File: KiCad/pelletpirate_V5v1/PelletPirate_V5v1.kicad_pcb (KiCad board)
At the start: 2 copper layers, 65 x 110 mm, 136 parts, among them J1 SJ1-3523NG_Jack_PP, J2 SJ1-3523NG_Jack_PP, J3 SJ1-3523NG_Jack_PP, J4 SJ1-3523NG_Jack_PP, J5 SJ1-3523NG_Jack_PP, J6 Conn_01x04, J7 Conn_01x04_Socket, J8 USB4145-03-0170-C, J9 TB002-500-02BE, T1 BTA12-600BWRG, T2 BTA12-600BWRG, T3 BTA12-600BWRG, U1 USBLC6-2SC6, U3 H11AA1M

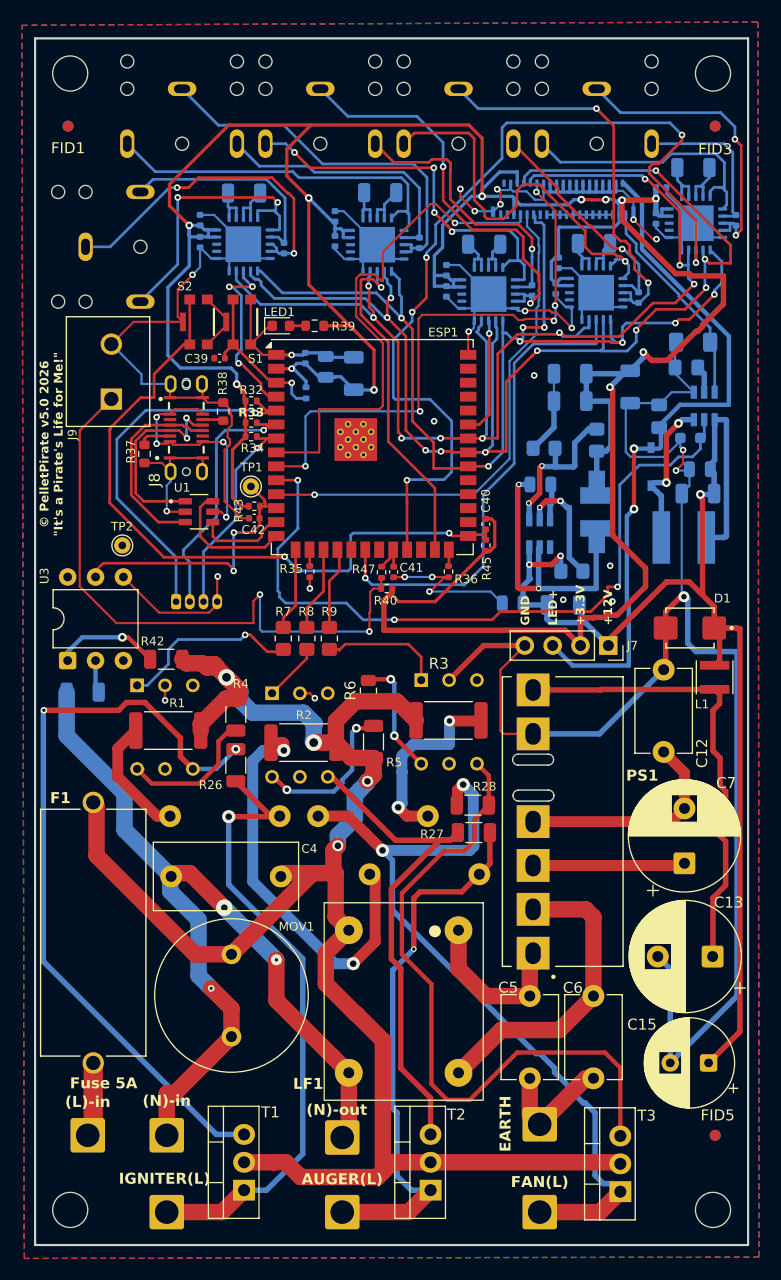
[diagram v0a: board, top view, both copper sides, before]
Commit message: V5v1 re-cloned fresh from as-ordered V5 (supersedes stale 80a9e8e clone)
V5 = frozen as-sent-to-PCBWay reference; V5v1 = working copy for all future tweaks.
Core files renamed + all internal refs patched (142 pcb sheetfile, 203 sch project,
pro meta/sheets/bom-path now local). Excluded: backups, archive_to_delete, PCBWay pkg.
ENHANCEMENT_BACKLOG carried over. Verified from new dir: ERC 0, DRC 0, unconnected 0.

Co-Authored-By: Claude Fable 5 <noreply@anthropic.com>
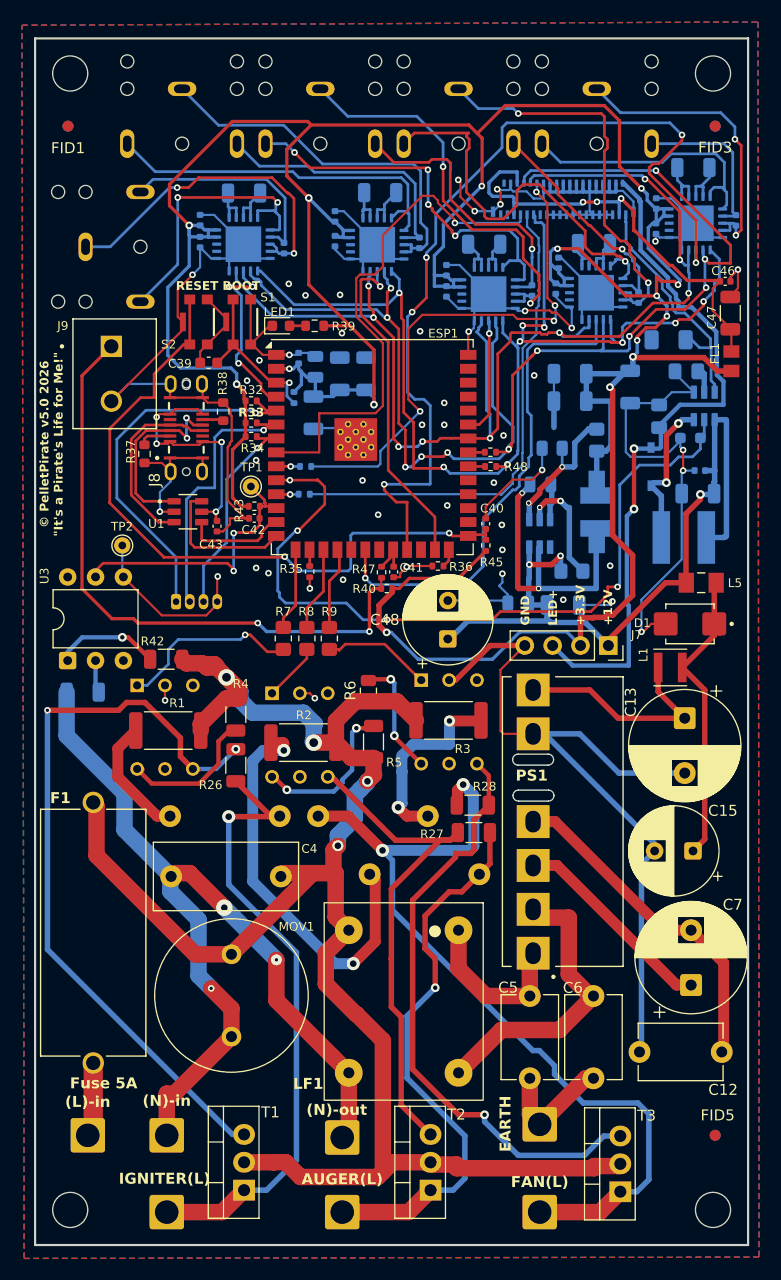
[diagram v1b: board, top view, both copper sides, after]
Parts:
- added C43: 0.1µF 25V, Capacitor_SMD:C_0402_1005Metric, F.Cu at (136.6, 84.5)
- added C44: 22µF 16V, Capacitor_SMD:C_1206_3216Metric, B.Cu at (147.8, 70.6)
- added C45: 22µF 16V, Capacitor_SMD:C_1206_3216Metric, B.Cu at (150.2, 70.6)
- added C46: 0.1µF 16V, Capacitor_SMD:C_0402_1005Metric, F.Cu at (182.9, 62.1)
- added C47: 22µF 16V, Capacitor_SMD:C_1206_3216Metric, F.Cu at (183.4, 65.0)
- added C48: 220µF 35V, Capacitor_THT:CP_Radial_D8.0mm_P3.50mm, F.Cu at (157.6, 94.8)
- added FL1: BLM21PG221SN1D, Ferrite_Bead:BEADC2012X105N, F.Cu at (183.5, 69.4)
- added L5: BLM31PG601SN1L, Ferrite_Bead_12V_Flyman:BEADC3216X130N_flyman, F.Cu at (180.7, 89.6)
- added R48: 33Ω, Resistor_SMD:R_0402_1005Metric, F.Cu at (161.5, 79.0)
- added R49: 33Ω, Resistor_SMD:R_0402_1005Metric, F.Cu at (161.5, 77.7)
- added R50: 33Ω, Resistor_SMD:R_0402_1005Metric, B.Cu at (144.7, 79.0)
- added R51: 33Ω, Resistor_SMD:R_0402_1005Metric, B.Cu at (144.5, 81.5)
- C39: value 0.1µF 25V -> 1.0µF 25V; footprint Capacitor_SMD:C_0402_1005Metric -> Capacitor_SMD:C_0603_1608Metric
- C9: footprint Capacitor_SMD:C_0805_2012Metric -> Capacitor_SMD:C_0402_1005Metric
- R20: footprint Resistor_SMD:R_0805_2012Metric_Pad1.20x1.40mm_HandSolder -> Resistor_SMD:R_0805_2012Metric
- moved C12 27.9 mm to (182.6, 132.4), turned to 180 degrees
- moved C13 21.9 mm to (179.2, 102.0), turned to -90 degrees
- moved C15 19.4 mm to (180.0, 114.1)
- moved C7 11.1 mm to (179.8, 126.3)
- moved C38 5.13 mm to (145.4, 74.1), turned to -90 degrees
- moved J9 4.80 mm to (127.0, 68.1), turned to -90 degrees
- moved L1 4.15 mm to (177.9, 97.3), turned to 0 degrees
- moved R17 2.25 mm to (177.8, 67.5)
- moved C35 1.52 mm to (176.6, 55.1), turned to -90 degrees
- moved R44 1.18 mm to (143.6, 72.7)
- moved R36 1.09 mm to (156.7, 88.1), turned to 180 degrees
- moved C39 1.08 mm to (135.8, 69.6)
- moved U1 1.01 mm to (133.9, 83.2)
- moved C37 0.95 mm to (145.6, 70.0)
- moved C25 0.92 mm to (176.6, 57.3)
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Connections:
- C15 pad 1: +12V -> Net-(C15-Pad1)
- C40 pad 2: +3.3V -> GND
- D1 pad 1: +12V -> Net-(C15-Pad1)
- ESP1 pad 11: /LCD_DC -> Net-(ESP1-IO18)
- ESP1 pad 32: /ALL_SDI -> Net-(ESP1-IO39)
- ESP1 pad 33: /ALL_SCLK -> Net-(ESP1-IO40)
- ESP1 pad 9: /LCD_CS -> Net-(ESP1-IO16)
- FPC1 pad 3: +3.3V -> /3V3_LCD
- FPC1 pad 34: +3.3V -> /3V3_LCD
- FPC1 pad 35: +3.3V -> /3V3_LCD
- L1 pad 2: +12V -> Net-(C15-Pad1)
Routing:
- net +12V: track 114.3 -> 71.3 mm
- net /3V3_LCD: track 0.00 -> 41.0 mm, vias 0 -> 3
- net Net-(C15-Pad1): track 0.00 -> 28.0 mm
- net Net-(PS1-+VO): track 43.8 -> 20.5 mm
- net Net-(PS1--V(CAP)): track 20.5 -> 31.5 mm
- net +3.3V: track 309.2 -> 316.1 mm, vias 12 -> 15
- net Net-(T3-G): track 61.5 -> 55.3 mm, vias 0 -> 1
- net Net-(T3-A1): track 72.8 -> 78.3 mm
- net /ALL_SCLK: track 114.9 -> 120.2 mm, vias 10 -> 11
- net Net-(PS1-+V(CAP)): track 13.9 -> 18.9 mm
- net /LCD_CS: track 52.6 -> 48.1 mm, vias 5 -> 4
- net /ALL_SDI: track 97.7 -> 101.1 mm, vias 8 -> 9
- net /LED_PWM: track 67.7 -> 71.0 mm, vias 3 -> 4
- net /LED-: track 19.6 -> 22.6 mm
- net GND: track 380.3 -> 377.4 mm, vias 27 -> 47
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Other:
- board text added: "BOOT"
- board text added: "RESET"
